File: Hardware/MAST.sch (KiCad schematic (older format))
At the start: 122 parts, among them J1 S+, J2 S-, J3 S-, J4 BAT+, J5 BAT-, Q1 DMP21D0UFB4, Q2 PMZ290UNE2, U1 LP5907SNX-3.0, U2 TPS62748, U3 ARTIC-R2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

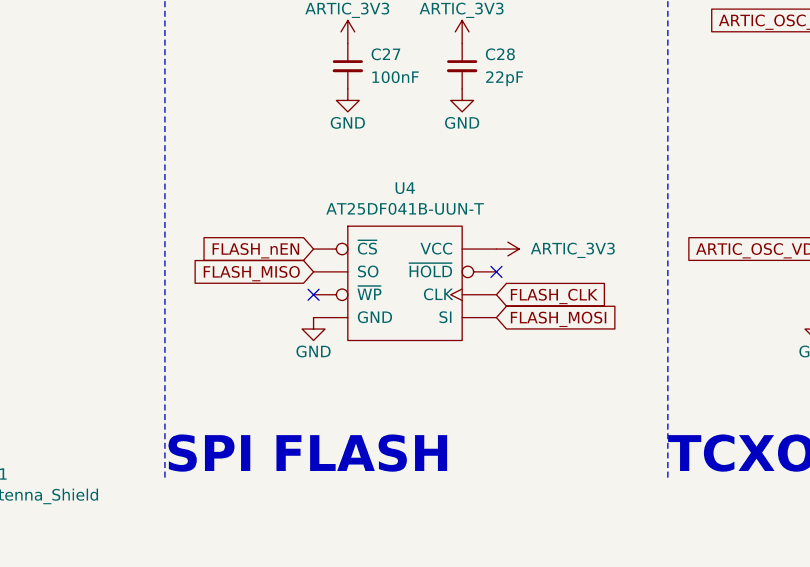
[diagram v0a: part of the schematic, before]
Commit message: Fix flash chip orientation
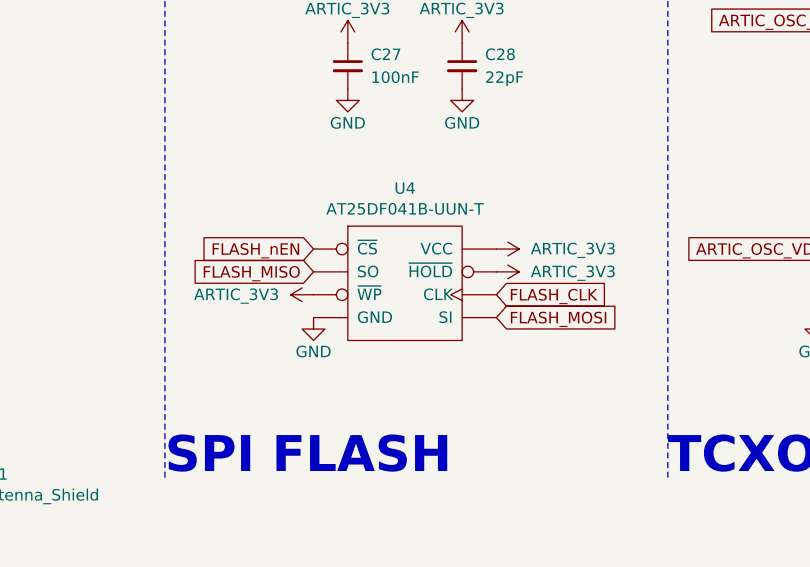
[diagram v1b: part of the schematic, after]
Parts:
- U4: Digikey# 1265-1222-2-ND -> (none); LCSC# - -> (none); Manufacturer Adesto -> (none); Part# AT25DF041B-UUN-T -> (none)
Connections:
- net ARTIC_3V3: now also U4.C1 (~HOLD), U4.E3 (~WP)
- no-connect marks 20 -> 18
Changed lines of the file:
@@
-$EndComp
-$Comp
-L MAST:AT25DF041B-UUN-T U4
-U 1 1 60859090
-P 12850 9100
-F 0 "U4" H 12850 9515 50  0000 C CNN
-F 1 "AT25DF041B-UUN-T" H 12850 9424 50  0000 C CNN
-F 2 "Package_CSP:WLCSP-8_1.58x1.63x0.35mm_Layout3x5_P0.35x0.4mm_Ball0.25mm_Pad0.25mm_NSMD" H 12850 9100 50  0001 C CNN
-F 3 "" H 13100 9150 50  0001 C CNN
-F 4 "1265-1222-2-ND" H 12850 9100 50  0001 C CNN "Digikey#"
-F 5 "-" H 12850 9100 50  0001 C CNN "LCSC#"
-F 6 "Adesto" H 12850 9100 50  0001 C CNN "Manufacturer"
-F 7 "AT25DF041B-UUN-T" H 12850 9100 50  0001 C CNN "Part#"
-	1    12850 9100
-	1    0    0    -1
 $EndComp
 $Comp
@@
 Text Notes 1850 4400 0    50   ~ 0
 10 Pin ARM SWD
-NoConn ~ 12450 9150
-NoConn ~ 13250 9050
 $Comp
 L Device:R_US R3
@@
 	1    0    0    -1
 $EndComp
+$Comp
+L MAST:AT25DF041B-UUN-T U4
+U 1 1 60F8A8F5
+P 12850 9100
+F 0 "U4" H 12850 9515 50  0000 C CNN
+F 1 "AT25DF041B-UUN-T" H 12850 9424 50  0000 C CNN
+F 2 "Package_CSP:WLCSP-8_1.58x1.63x0.35mm_Layout3x5_P0.35x0.4mm_Ball0.25mm_Pad0.25mm_NSMD" H 12850 9100 50  0001 C CNN
+F 3 "" H 13100 9150 50  0001 C CNN
+	1    12850 9100
+	1    0    0    -1
+$EndComp
+$Comp
+L MAST:ARTIC_3V3 #PWR0123
+U 1 1 60F8BE31
+P 13250 9050
+F 0 "#PWR0123" H 13250 8900 50  0001 C CNN
+F 1 "ARTIC_3V3" V 13250 9200 50  0000 L CNN
+F 2 "" H 13250 9050 50  0001 C CNN
+F 3 "" H 13250 9050 50  0001 C CNN
+	1    13250 9050
+	0    1    1    0
+$EndComp
+$Comp
+L MAST:ARTIC_3V3 #PWR0124
+U 1 1 60F9DD77
+P 12450 9150
+F 0 "#PWR0124" H 12450 9000 50  0001 C CNN
+F 1 "ARTIC_3V3" V 12450 9300 50  0000 L CNN
+F 2 "" H 12450 9150 50  0001 C CNN
+F 3 "" H 12450 9150 50  0001 C CNN
+	1    12450 9150
+	0    -1   -1   0
+$EndComp
 $EndSCHEMATC

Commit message: Enable MPPC on solar charger
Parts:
- added R12: MPPC_SET, Resistor_SMD:R_0603_1608Metric, symbol Device:R_US
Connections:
- net GND: now also R12.2; no longer U9.5 (MPPC)
- new net: R12.1, U9.5 (MPPC)
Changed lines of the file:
@@
 NoConn ~ 3250 2150
-$Comp
-L power:GND #PWR0112
-U 1 1 6093A1E1
-P 3250 2050
-F 0 "#PWR0112" H 3250 1800 50  0001 C CNN
-F 1 "GND" V 3250 1900 50  0000 R CNN
-F 2 "" H 3250 2050 50  0001 C CNN
-F 3 "" H 3250 2050 50  0001 C CNN
-	1    3250 2050
-	0    1    1    0
-$EndComp
 $Comp
 L power:GND #PWR0114
@@
 	0    -1   -1   0
 $EndComp
+$Comp
+L Device:R_US R12
+U 1 1 60F42FFC
+P 2550 2400
+F 0 "R12" H 2618 2446 50  0000 L CNN
+F 1 "MPPC_SET" H 2618 2355 50  0000 L CNN
+F 2 "Resistor_SMD:R_0603_1608Metric" V 2590 2390 50  0001 C CNN
+F 3 "~" H 2550 2400 50  0001 C CNN
+F 4 "" H 2550 2400 50  0001 C CNN "Digikey#"
+F 5 "" H 2550 2400 50  0001 C CNN "LCSC#"
+F 6 "" H 2550 2400 50  0001 C CNN "Manufacturer"
+F 7 "" H 2550 2400 50  0001 C CNN "Part#"
+	1    2550 2400
+	1    0    0    -1
+$EndComp
+$Comp
+L power:GND #PWR0112
+U 1 1 60F462A1
+P 2550 2550
+F 0 "#PWR0112" H 2550 2300 50  0001 C CNN
+F 1 "GND" H 2550 2400 50  0000 C CNN
+F 2 "" H 2550 2550 50  0001 C CNN
+F 3 "" H 2550 2550 50  0001 C CNN
+	1    2550 2550
+	1    0    0    -1
+$EndComp
+Wire Wire Line
+	3250 2050 2550 2050
+Wire Wire Line
+	2550 2050 2550 2250
 $EndSCHEMATC
